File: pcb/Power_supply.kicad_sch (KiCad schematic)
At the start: 33 parts, among them Q1 Si4368DY, SW1 POWER, U1 LTC3872, U2 uA78M33

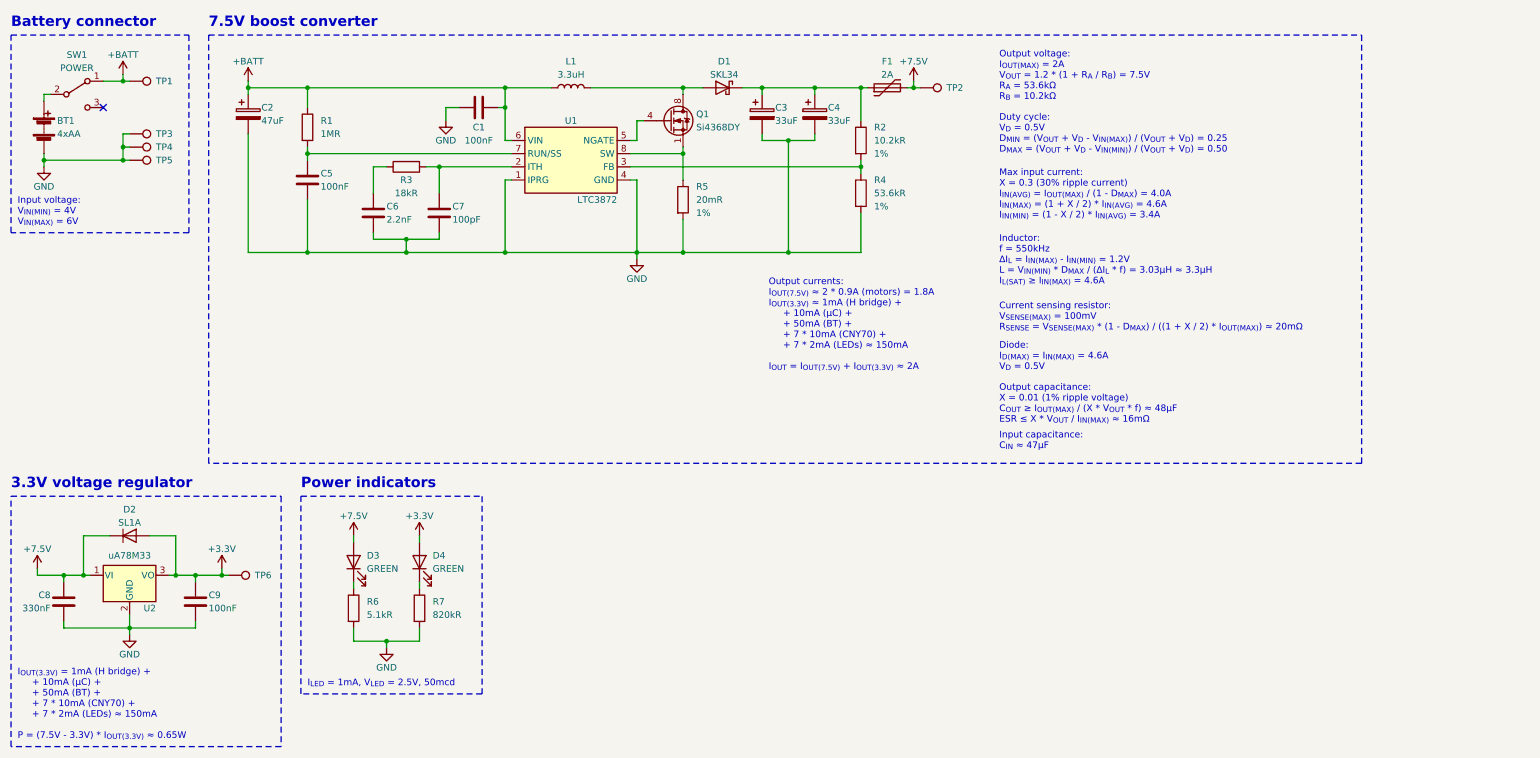
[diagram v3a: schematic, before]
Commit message: [pcb] ERC/DRC checks
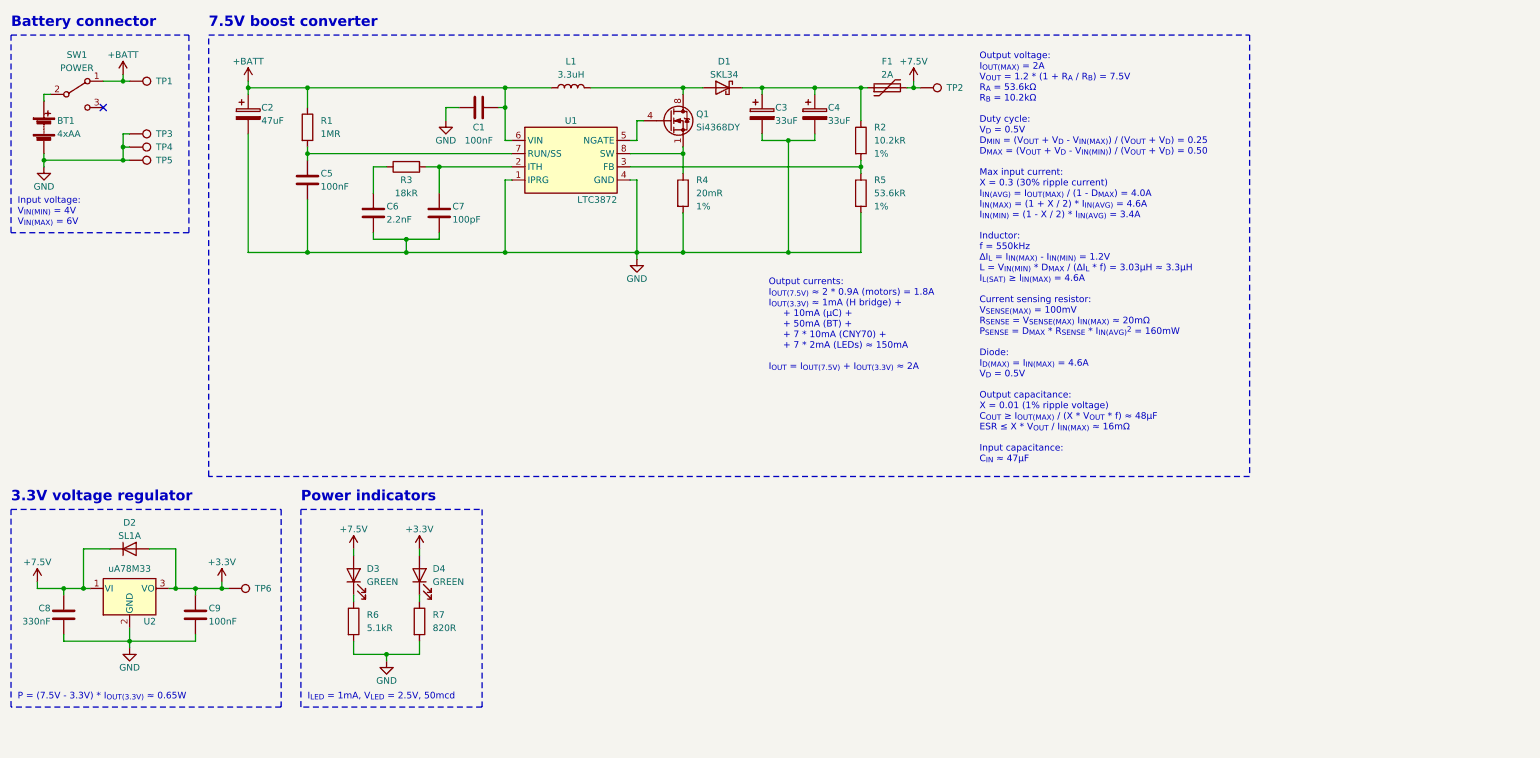
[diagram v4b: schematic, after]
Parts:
- R7: value 820kR -> 820R
- renumbered R5 to R4, R4 to R5
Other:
- note added: "Output voltage: I_{OUT(MAX)} = 2A V_{OUT} = 1.2 * (1 + R_{A} / R_{B}) = 7.5V R_{A} = 53.6kΩ R_{B} = 10.2kΩ Duty cycle: V_{D} = 0.5V D_{MIN} = (V_{OUT} + V_{D} - V_{IN(MAX)}) / (V_{OUT} + V_{D}) = 0.25 D_{MAX} = (V_{OUT} + V_{D} - V_{IN(MIN)}) / (V_{OUT} + V_{D}) = 0.50 Max input current: X = 0.3 (30% ripple current) I_{IN(AVG)} = I_{OUT(MAX)} / (1 - D_{MAX}) = 4.0A I_{IN(MAX)} = (1 + X / 2) * I_{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"
- note added: "P = (7.5V - 3.3V) * I_{OUT(3.3V)} ≈ 0.65W"
- note removed: "Current sensing resistor: V_{SENSE(MAX)} = 100mV R_{SENSE} = V_{SENSE(MAX)} * (1 - D_{MAX}) / ((1 + X / 2) * I_{OUT(MAX)}) ≈ 20mΩ"
- note removed: "Diode: I_{D(MAX)} = I_{IN(MAX)} = 4.6A V_{D} = 0.5V"
- note removed: "Duty cycle: V_{D} = 0.5V D_{MIN} = (V_{OUT} + V_{D} - V_{IN(MAX)}) / (V_{OUT} + V_{D}) = 0.25 D_{MAX} = (V_{OUT} + V_{D} - V_{IN(MIN)}) / (V_{OUT} + V_{D}) = 0.50"
- note removed: "I_{OUT(3.3V)} = 1mA (H bridge) + + 10mA (µC) + + 50mA (BT) + + 7 * 10mA (CNY70) + + 7 * 2mA (LEDs) ≈ 150mA P = (7.5V - 3.3V) * I_{OUT(3.3V)} ≈ 0.65W"
- note removed: "Inductor: f = 550kHz ∆I_{L} = I_{IN(MAX)} - I_{IN(MIN)} = 1.2V L = V_{IN(MIN)} * D_{MAX} / (∆I_{L} * f) = 3.03μH ≈ 3.3μH I_{L(SAT)} ≥ I_{IN(MAX)} = 4.6A"
- note removed: "Input capacitance: C_{IN} ≈ 47μF"
- note removed: "Max input current: X = 0.3 (30% ripple current) I_{IN(AVG)} = I_{OUT(MAX)} / (1 - D_{MAX}) = 4.0A I_{IN(MAX)} = (1 + X / 2) * I_{IN(AVG)} = 4.6A I_{IN(MIN)} = (1 - X / 2) * I_{IN(AVG)} = 3.4A"
- note removed: "Output capacitance: X = 0.01 (1% ripple voltage) C_{OUT} ≥ I_{OUT(MAX)} / (X * V_{OUT} * f) ≈ 48μF ESR ≤ X * V_{OUT} / I_{IN(MAX)} ≈ 16mΩ"
- note removed: "Output voltage: I_{OUT(MAX)} = 2A V_{OUT} = 1.2 * (1 + R_{A} / R_{B}) = 7.5V R_{A} = 53.6kΩ R_{B} = 10.2kΩ"
- moved on the sheet: C8, C9, D2, D3, D4, R4, R6, R7, TP6, U2
